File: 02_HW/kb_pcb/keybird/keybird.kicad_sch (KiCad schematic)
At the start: 73 parts, among them J1 Adafruit_Feather_16_pin, J2 Adafruit_feather_12_pin, J3 UART, SW1 SW_Push, SW10 SW_Push, SW11 SW_Push, SW12 SW_Push, SW13 SW_Push, SW14 SW_Push, SW15 SW_Push, SW16 SW_Push, SW17 SW_Push, SW18 SW_Push, SW19 SW_Push, SW2 SW_Push, SW20 SW_Push, SW21 SW_Push, SW22 SW_Push, SW23 SW_Push, SW24 SW_Push, SW25 SW_Push, SW26 SW_Push, SW27 SW_Push, SW28 SW_Push, SW29 SW_Push, SW3 SW_Push, SW30 SW_Push, SW4 SW_Push, SW5 Power enable, SW6 SW_Push, SW7 SW_Push, SW8 SW_Push, SW9 SW_Push

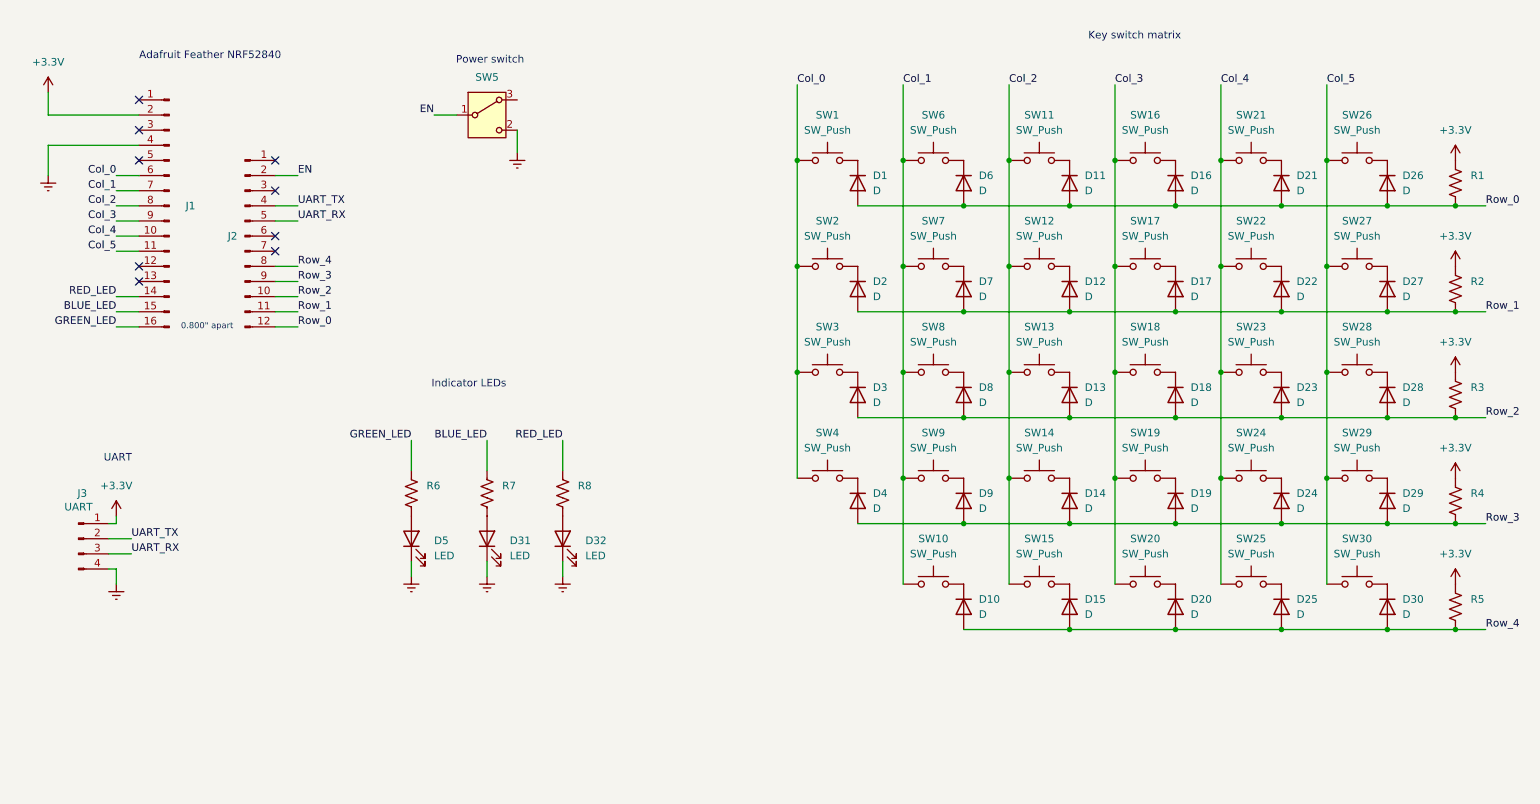
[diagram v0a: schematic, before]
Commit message: Updated uart connector to match ftdi cable pinout
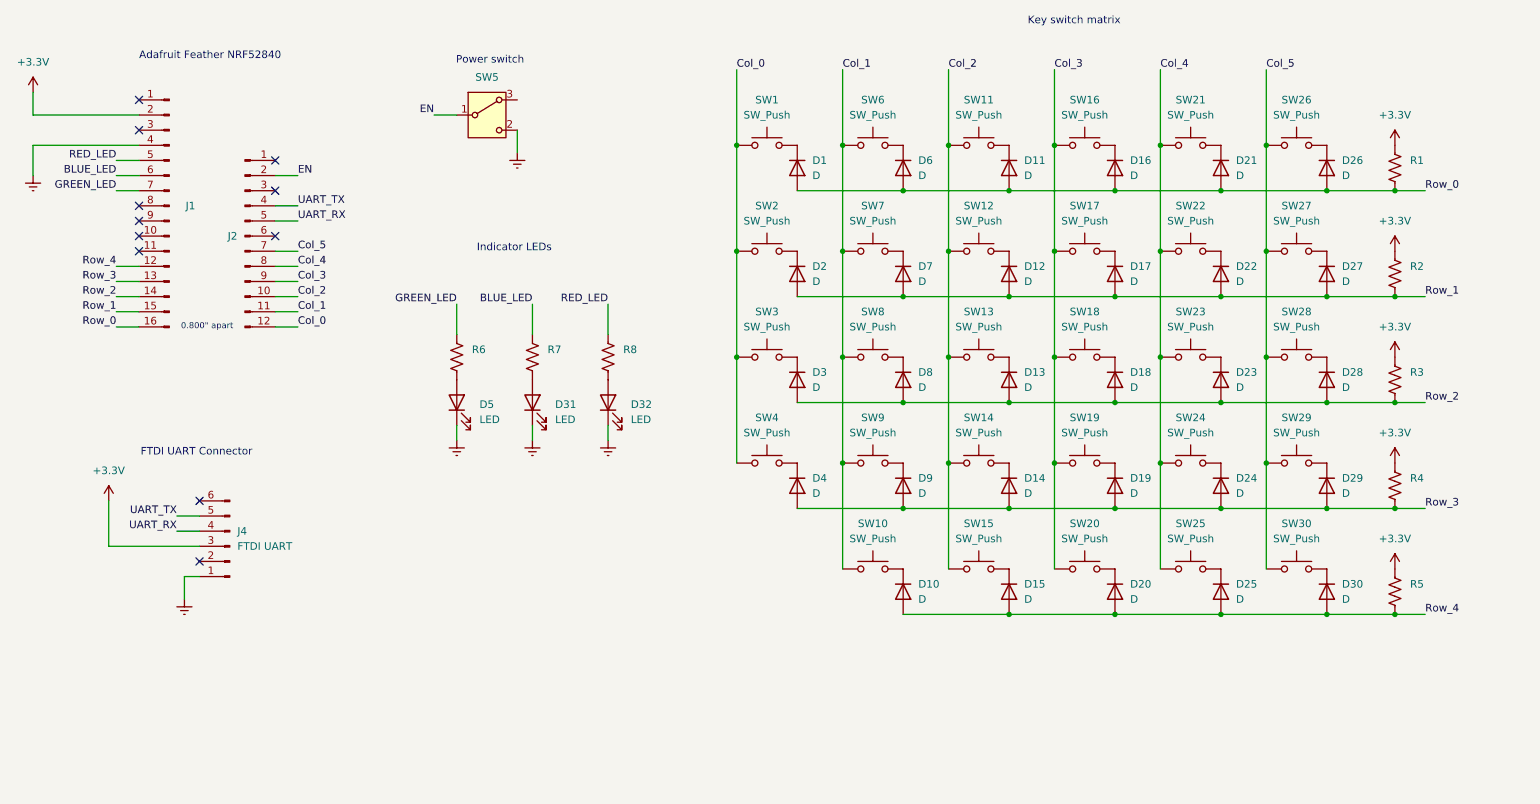
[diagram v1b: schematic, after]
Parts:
- removed J3: UART, symbol Connector:Conn_01x04_Pin
- added J4: FTDI UART, Connector_PinHeader_2.54mm:PinHeader_1x06_P2.54mm_Vertical, symbol Connector:Conn_01x06_Pin
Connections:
- net +3.3V: now also J4.3 (Pin_3)
- net BLUE_LED: now also J1.6 (Pin_6); no longer J1.15 (Pin_15)
- net Col_0: now also J2.12 (Pin_12); no longer J1.6 (Pin_6)
- net Col_1: now also J2.11 (Pin_11); no longer J1.7 (Pin_7)
- net Col_2: now also J2.10 (Pin_10); no longer J1.8 (Pin_8)
- net Col_3: now also J2.9 (Pin_9); no longer J1.9 (Pin_9)
- net Col_4: now also J2.8 (Pin_8); no longer J1.10 (Pin_10)
- net Col_5: now also J2.7 (Pin_7); no longer J1.11 (Pin_11)
- net GNDREF: now also J4.1 (Pin_1)
- net GREEN_LED: now also J1.7 (Pin_7); no longer J1.16 (Pin_16)
- net RED_LED: now also J1.5 (Pin_5); no longer J1.14 (Pin_14)
- net Row_0: now also J1.16 (Pin_16); no longer J2.12 (Pin_12)
- net Row_1: now also J1.15 (Pin_15); no longer J2.11 (Pin_11)
- net Row_2: now also J1.14 (Pin_14); no longer J2.10 (Pin_10)
- net Row_3: now also J1.13 (Pin_13); no longer J2.9 (Pin_9)
- net Row_4: now also J1.12 (Pin_12); no longer J2.8 (Pin_8)
- net UART_RX: now also J4.4 (Pin_4)
- net UART_TX: now also J4.5 (Pin_5)
- no-connect marks 9 -> 11
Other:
- note added: "FTDI UART Connector"
- note removed: "UART"
- moved on the sheet: D1, D10, D11, D12, D13, D14, D15, D16, D17, D18, D19, D2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

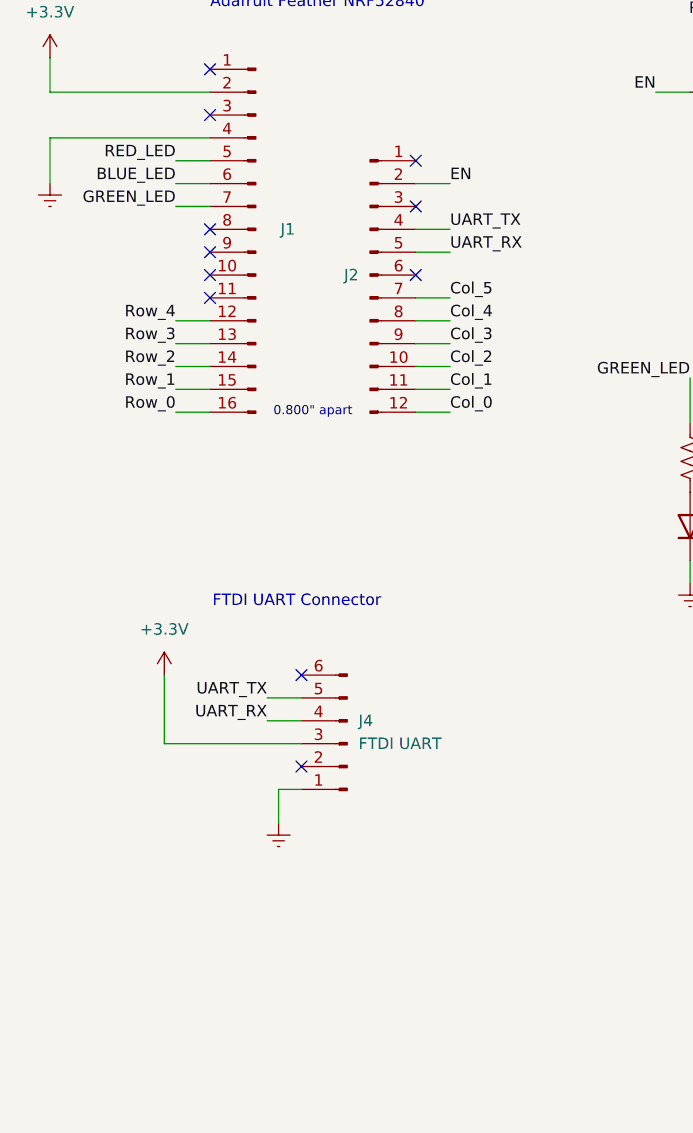
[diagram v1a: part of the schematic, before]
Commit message: Trimmed down board shape, completed tracing, adding ground pours and via stitching
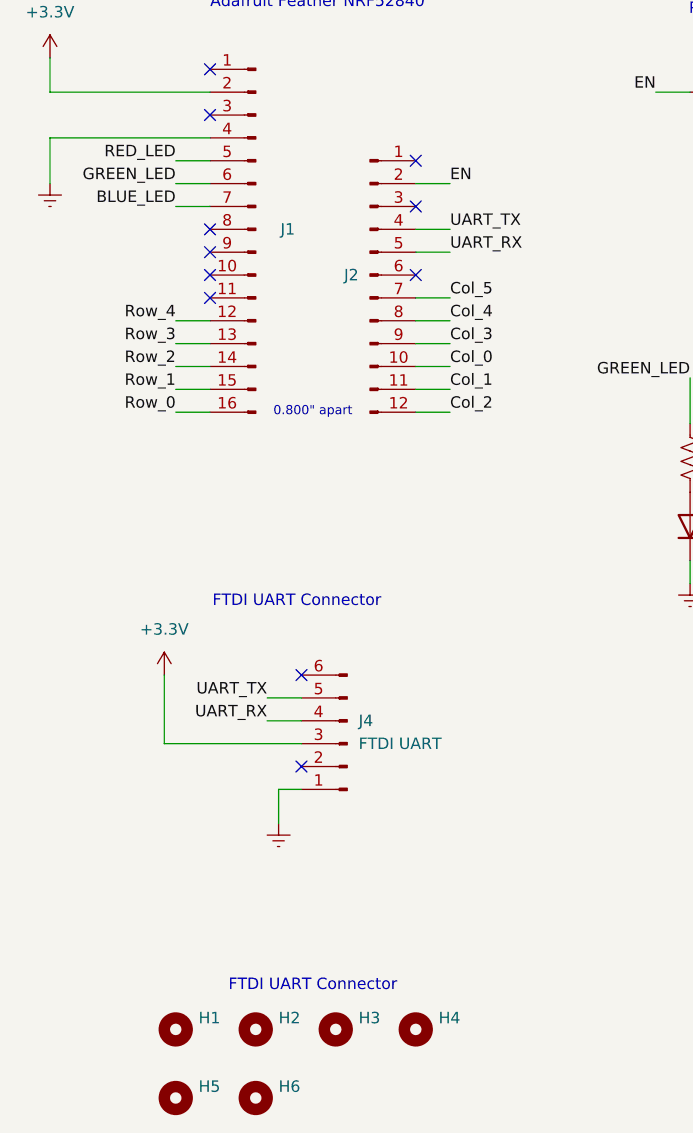
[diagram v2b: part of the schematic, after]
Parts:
- added H1, H2, H3, H4, H5, H6: MountingHole, MountingHole:MountingHole_2.5mm, symbol Mechanical:MountingHole
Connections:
- net BLUE_LED: now also J1.7 (Pin_7); no longer J1.6 (Pin_6)
- net Col_0: now also J2.10 (Pin_10); no longer J2.12 (Pin_12)
- net Col_2: now also J2.12 (Pin_12); no longer J2.10 (Pin_10)
- net GREEN_LED: now also J1.6 (Pin_6); no longer J1.7 (Pin_7)

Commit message: Resolved design rule conflicts
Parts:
- J1: footprint Connector_PinSocket_2.54mm:PinSocket_1x16_P2.54mm_Vertical -> Connector_PinHeader_2.54mm:PinHeader_1x16_P2.54mm_Vertical
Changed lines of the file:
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@@
 			)
 		)
-		(property "Footprint" "Connector_PinSocket_2.54mm:PinSocket_1x16_P2.54mm_Vertical"
+		(property "Footprint" "Connector_PinHeader_2.54mm:PinHeader_1x16_P2.54mm_Vertical"
 			(at 43.18 66.04 0)
 			(effects
